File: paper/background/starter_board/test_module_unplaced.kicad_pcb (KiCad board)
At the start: 2 copper layers, 82.3 x 112.9 mm, 14 parts, among them J1 Barrel_Jack_12V, M1 ERM_Motor, M2 Stepper_4wire, M3 Servo_3pin, U1 D24V22F5_Buck, U2 Pi_Pico_W, U3 DRV2605L_Breakout, U4 DRV8871_Breakout, U5 Tic_T500

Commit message: Compact starter-board placement + emit unplaced auto-place variant trio
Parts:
- moved U3 94.3 mm to (157.2, 22.3)
- moved C3 94.3 mm to (128.3, 79.0)
- moved J1 94.3 mm to (101.8, 6.00)
- moved M1 94.3 mm to (100.4, 50.0)
- moved M2 94.3 mm to (100.4, 96.8)
- moved M3 94.3 mm to (114.3, 98.1)
- moved SR1 94.3 mm to (148.6, 79.8)
- moved U1 94.3 mm to (117.6, 5.58)
- moved U2 94.3 mm to (120.3, 29.8)
- moved U4 94.3 mm to (118.8, 60.2)
- moved U5 94.3 mm to (107.5, 83.0)
- moved C1 94.3 mm to (132.1, 4.75)
- moved C2 94.3 mm to (146.0, 4.75)
- moved SOL1 94.3 mm to (137.1, 50.0)
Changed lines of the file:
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@@
   (net 20 "VIB_B")
   (footprint "powder_doser_parts:Barrel_Jack_12V" (version 20221018) (generator kiutils) (layer "F.Cu")
-    (at 7.5 6.0 0)
+    (at 101.78 6.0 0)
     (fp_text reference "J1" (at 0 -6.5 0) (layer "F.SilkS")
       (effects (font (size 1.0 1.0) (thickness 0.15)))
@@
   )
   (footprint "powder_doser_parts:D24V22F5_Buck" (version 20221018) (generator kiutils) (layer "F.Cu")
-    (at 23.35 5.58 0)
+    (at 117.63 5.58 0)
     (fp_text reference "U1" (at 0 -6.08 0) (layer "F.SilkS")
       (effects (font (size 1.0 1.0) (thickness 0.15)))
@@
   )
   (footprint "powder_doser_parts:Cap_Polar" (version 20221018) (generator kiutils) (layer "F.Cu")
-    (at 37.86 4.75 0)
+    (at 132.14 4.75 0)
     (fp_text reference "C1" (at 0 -5.25 0) (layer "F.SilkS")
       (effects (font (size 1.0 1.0) (thickness 0.15)))
@@
   )
   (footprint "powder_doser_parts:Cap_Polar" (version 20221018) (generator kiutils) (layer "F.Cu")
-    (at 51.67999999999999 4.75 0)
+    (at 145.95999999999998 4.75 0)
     (fp_text reference "C2" (at 0 -5.25 0) (layer "F.SilkS")
       (effects (font (size 1.0 1.0) (thickness 0.15)))
@@
   )
   (footprint "powder_doser_parts:Pi_Pico_W" (version 20221018) (generator kiutils) (layer "F.Cu")
-    (at 26.0 29.82 0)
+    (at 120.28 29.82 0)
     (fp_text reference "U2" (at 0 -16.82 0) (layer "F.SilkS")
       (effects (font (size 1.0 1.0) (thickness 0.15)))
@@
   )
   (footprint "powder_doser_parts:DRV2605L_Breakout" (version 20221018) (generator kiutils) (layer "F.Cu")
-    (at 62.89 22.255000000000003 0)
+    (at 157.17000000000002 22.255000000000003 0)
     (fp_text reference "U3" (at 0 -9.255 0) (layer "F.SilkS")
       (effects (font (size 1.0 1.0) (thickness 0.15)))
@@
   )
   (footprint "powder_doser_parts:ERM_Motor" (version 20221018) (generator kiutils) (layer "F.Cu")
-    (at 6.16 49.99 0)
+    (at 100.44 49.99 0)
     (fp_text reference "M1" (at 0 -2.85 0) (layer "F.SilkS")
       (effects (font (size 1.0 1.0) (thickness 0.15)))
@@
   )
   (footprint "powder_doser_parts:DRV8871_Breakout" (version 20221018) (generator kiutils) (layer "F.Cu")
-    (at 24.48 60.205 0)
+    (at 118.76 60.205 0)
     (fp_text reference "U4" (at 0 -13.065 0) (layer "F.SilkS")
       (effects (font (size 1.0 1.0) (thickness 0.15)))
@@
   )
   (footprint "powder_doser_parts:Solenoid" (version 20221018) (generator kiutils) (layer "F.Cu")
-    (at 42.8 49.99 0)
+    (at 137.07999999999998 49.99 0)
     (fp_text reference "SOL1" (at 0 -2.85 0) (layer "F.SilkS")
       (effects (font (size 1.0 1.0) (thickness 0.15)))
@@
   )
   (footprint "powder_doser_parts:Tic_T500" (version 20221018) (generator kiutils) (layer "F.Cu")
-    (at 13.2 82.97 0)
+    (at 107.48 82.97 0)
     (fp_text reference "U5" (at 0 -9.2 0) (layer "F.SilkS")
       (effects (font (size 1.0 1.0) (thickness 0.15)))
@@
   )
   (footprint "powder_doser_parts:Cap_Polar" (version 20221018) (generator kiutils) (layer "F.Cu")
-    (at 34.06 79.02 0)
+    (at 128.34 79.02 0)
     (fp_text reference "C3" (at 0 -5.25 0) (layer "F.SilkS")
       (effects (font (size 1.0 1.0) (thickness 0.15)))
@@
   )
   (footprint "powder_doser_parts:Shunt_Regulator" (version 20221018) (generator kiutils) (layer "F.Cu")
-    (at 54.285 79.85 0)
+    (at 148.565 79.85 0)
     (fp_text reference "SR1" (at 0 -6.08 0) (layer "F.SilkS")
       (effects (font (size 1.0 1.0) (thickness 0.15)))
@@
   )
   (footprint "powder_doser_parts:Stepper_4wire" (version 20221018) (generator kiutils) (layer "F.Cu")
-    (at 6.16 96.78999999999999 0)
+    (at 100.44 96.78999999999999 0)
     (fp_text reference "M2" (at 0 -4.12 0) (layer "F.SilkS")
       (effects (font (size 1.0 1.0) (thickness 0.15)))
@@
   )
   (footprint "powder_doser_parts:Servo_3pin" (version 20221018) (generator kiutils) (layer "F.Cu")
-    (at 19.98 98.05999999999999 0)
+    (at 114.26 98.05999999999999 0)
     (fp_text reference "M3" (at 0 -5.390000000000001 0) (layer "F.SilkS")
       (effects (font (size 1.0 1.0) (thickness 0.15)))

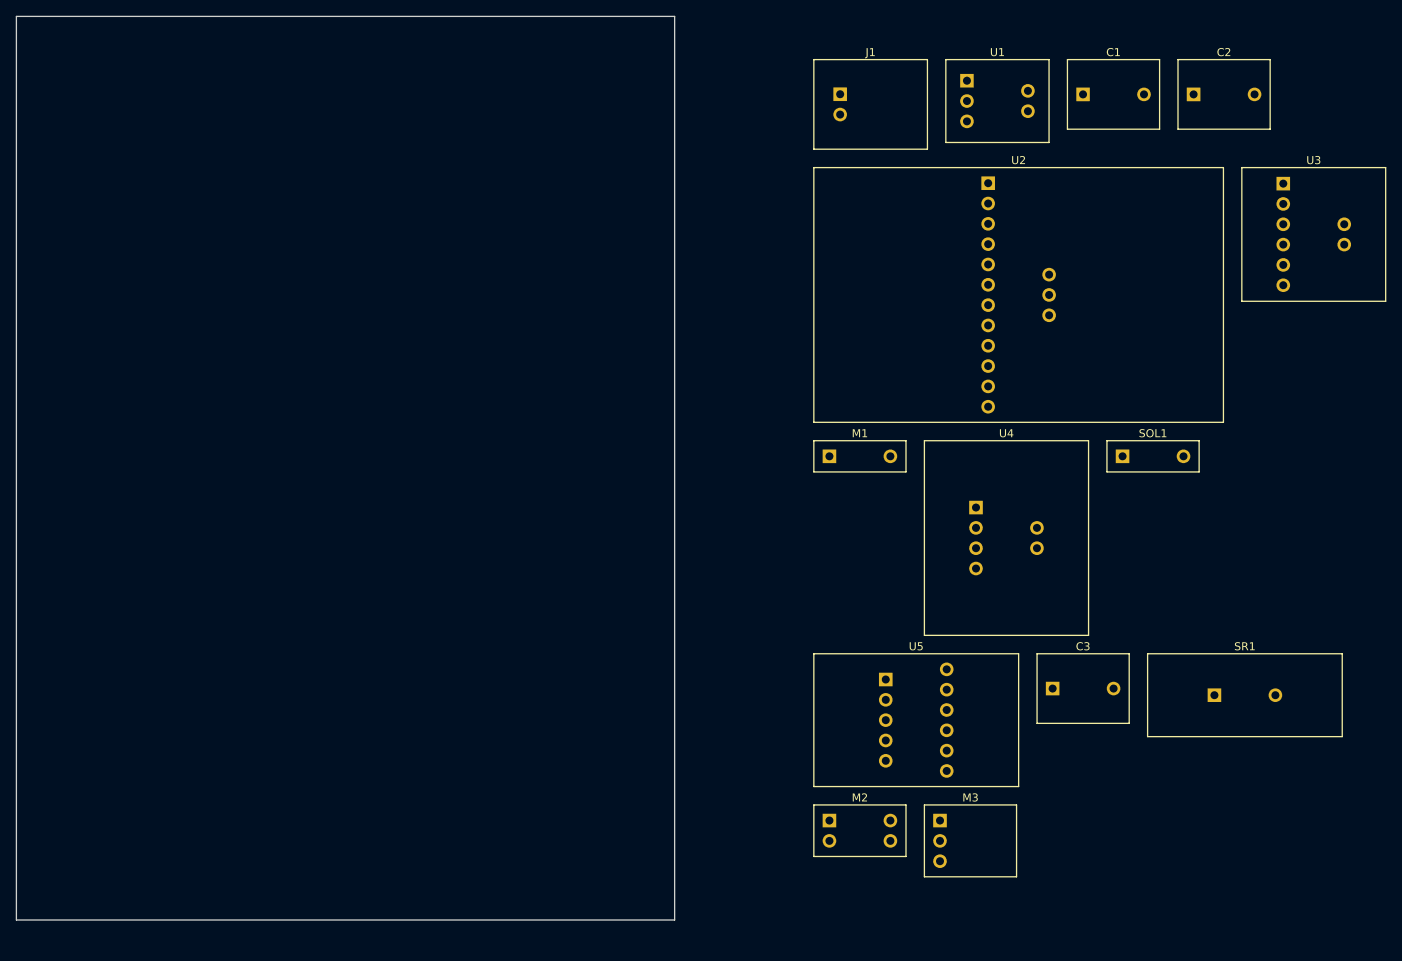
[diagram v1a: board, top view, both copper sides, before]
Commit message: Fix starter-board pin counts to match real parts (Pico W 15→40, etc.)
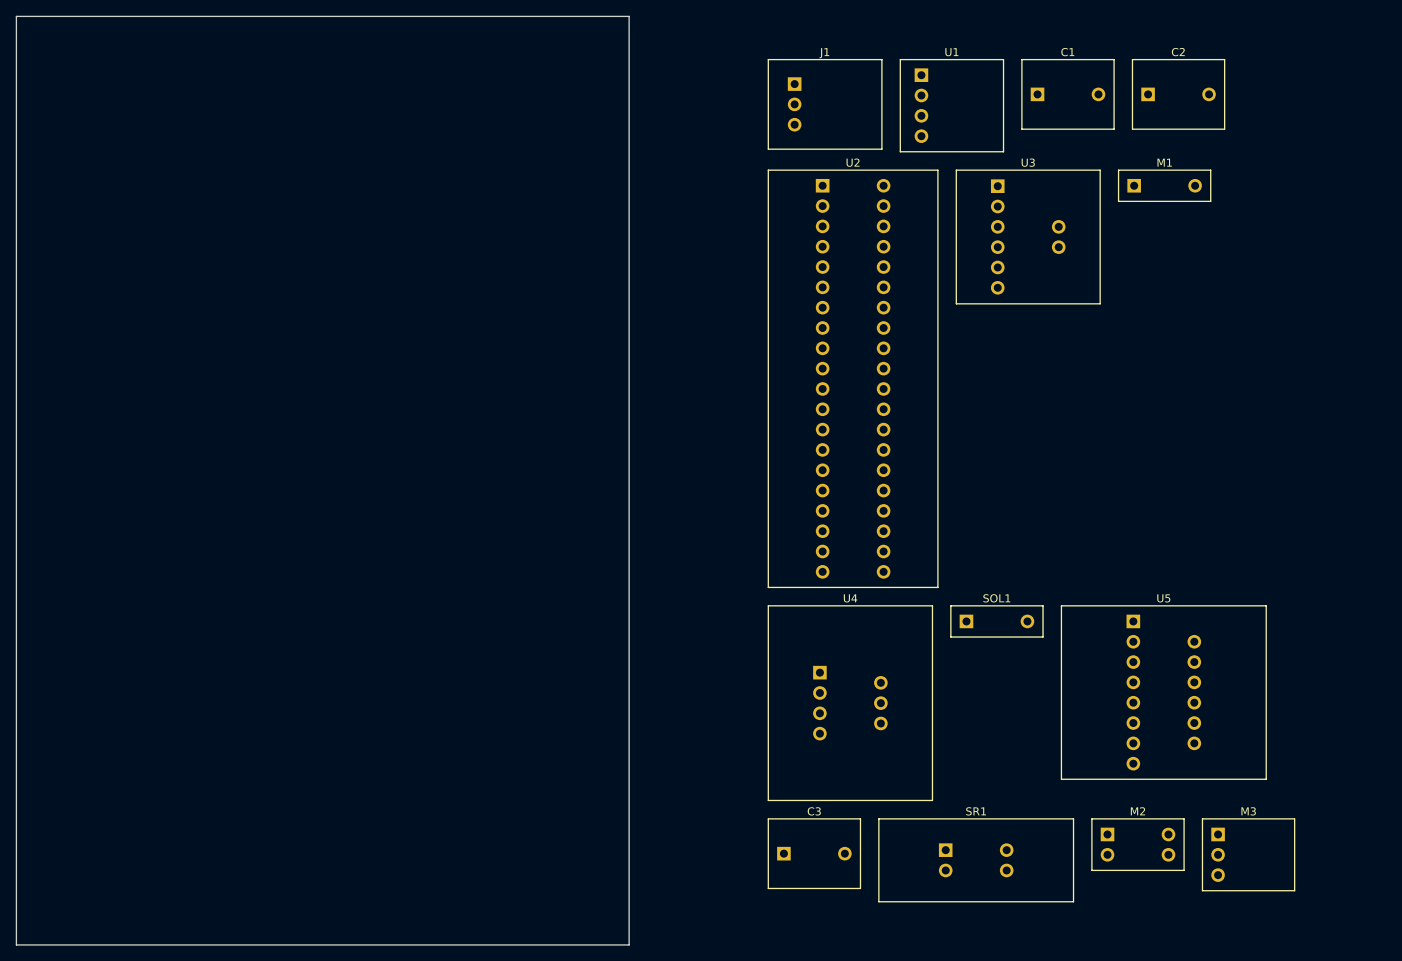
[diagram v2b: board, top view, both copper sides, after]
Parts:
- moved M1 50.9 mm to (138.5, 16.2)
- moved C3 39.4 mm to (94.8, 99.7)
- moved SR1 39.4 mm to (115.0, 100.5)
- moved U3 35.7 mm to (121.5, 22.6)
- moved M3 34.8 mm to (149.0, 99.8)
- moved M2 34.8 mm to (135.2, 98.5)
- moved U5 31.1 mm to (138.4, 79.5)
- moved U4 28.4 mm to (99.2, 80.8)
- moved SOL1 28.4 mm to (117.6, 70.6)
- moved U2 23.2 mm to (99.6, 40.3)
- moved U1 5.72 mm to (111.9, 6.16)
- moved C2 5.69 mm to (140.3, 4.75)
- moved J1 5.69 mm to (96.1, 6.00)
- moved C1 5.69 mm to (126.5, 4.75)
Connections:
- SR1 pad 2: GND -> +12V
- U1 pad 3: +12V -> +5V
- U1 pad 4: +5V -> +12V
- U2 pad 10: SOL_IN2 -> (no net)
- U2 pad 11: HAPT_EN -> (no net)
- U2 pad 12: SERVO_SIG -> (no net)
- U2 pad 13: +5V -> GND
- U2 pad 14: GND -> SOL_IN1
- U2 pad 15: +3V3 -> SOL_IN2
- U2 pad 3: (no net) -> GND
- U2 pad 5: STP_TX -> (no net)
- U2 pad 6: STP_RX -> STP_TX
- U2 pad 7: (no net) -> STP_RX
- U2 pad 8: (no net) -> GND
- U2 pad 9: SOL_IN1 -> (no net)
- U4 pad 3: SOL_IN1 -> SOL_A
- U4 pad 4: SOL_IN2 -> SOL_B
- U4 pad 5: SOL_A -> SOL_IN1
- U4 pad 6: SOL_B -> SOL_IN2
- U5 pad 10: STP_B1 -> GND
- U5 pad 11: STP_B2 -> STP_A1
- U5 pad 6: +12V -> (no net)
- U5 pad 8: STP_A1 -> (no net)
- U5 pad 9: STP_A2 -> +12V
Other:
- board size 82.3 x 112.9 mm -> 76.6 x 116.1 mm

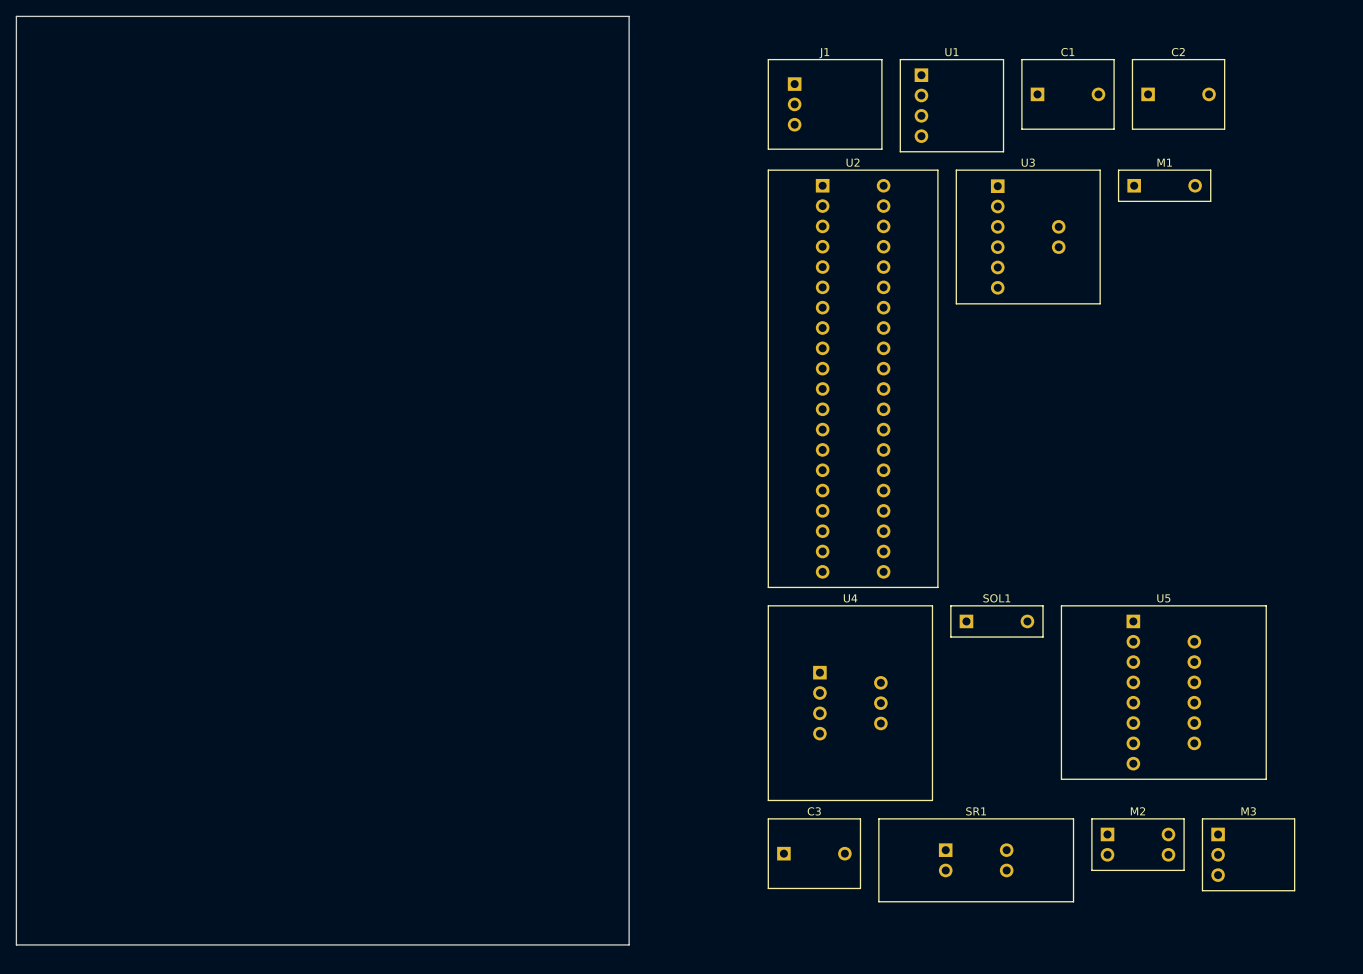
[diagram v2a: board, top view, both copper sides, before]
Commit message: Swap starter-board placeholder pads for real KiCad library footprints
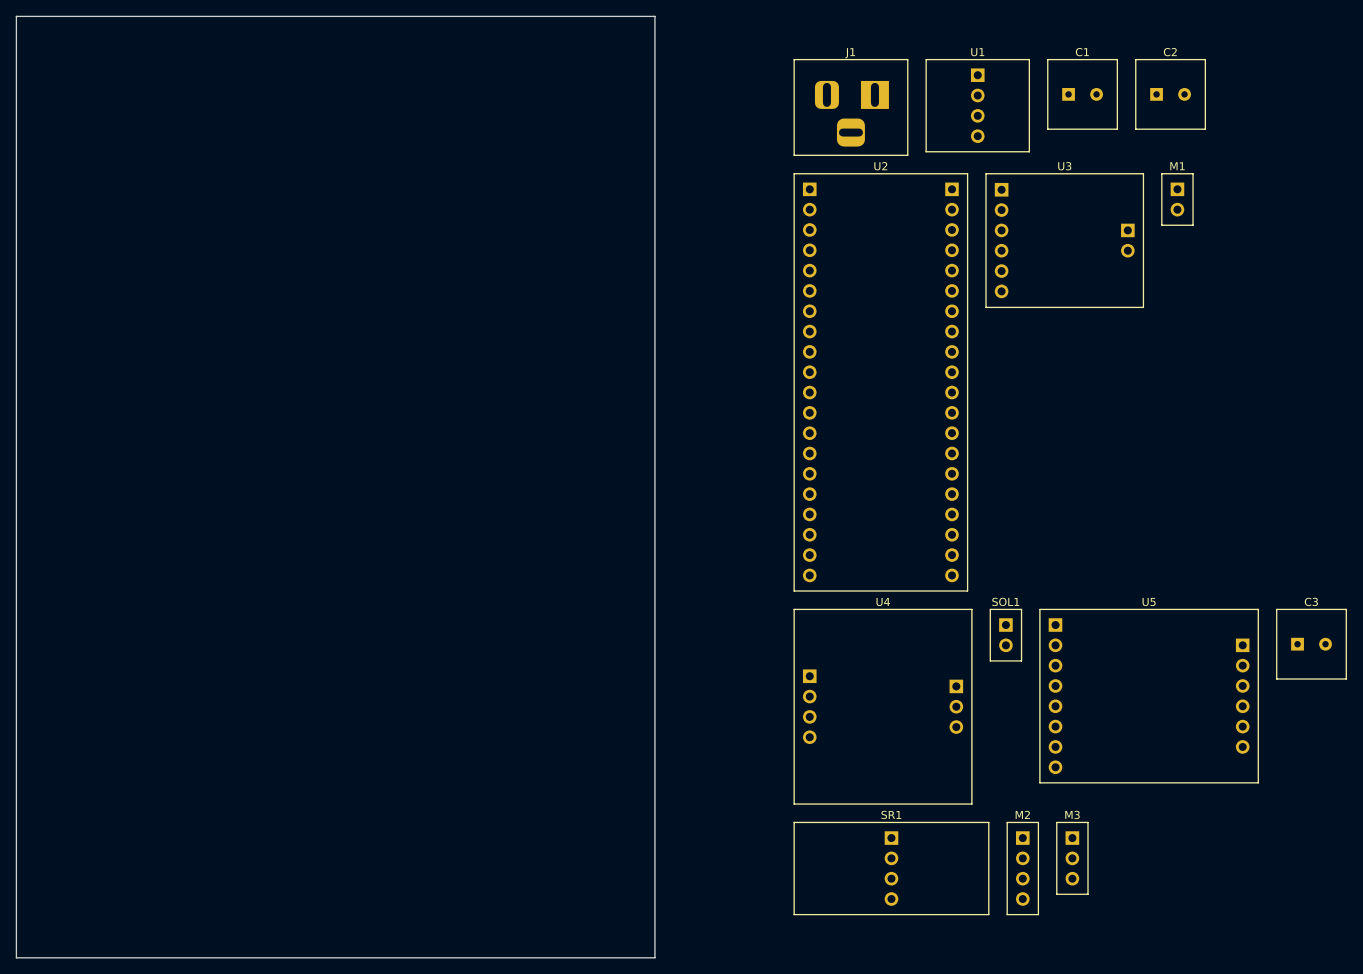
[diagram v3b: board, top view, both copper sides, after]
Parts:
- C1, C2, C3: footprint powder_doser_parts:Cap_Polar -> Capacitor_THT:CP_Radial_D8.0mm_P3.50mm
- J1: footprint powder_doser_parts:Barrel_Jack_12V -> Connector_BarrelJack:BarrelJack_Horizontal
- M1: footprint powder_doser_parts:ERM_Motor -> Connector_PinHeader_2.54mm:PinHeader_1x02_P2.54mm_Vertical
- M2: footprint powder_doser_parts:Stepper_4wire -> Connector_PinHeader_2.54mm:PinHeader_1x04_P2.54mm_Vertical
- M3: footprint powder_doser_parts:Servo_3pin -> Connector_PinHeader_2.54mm:PinHeader_1x03_P2.54mm_Vertical
- SOL1: footprint powder_doser_parts:Solenoid -> Connector_PinHeader_2.54mm:PinHeader_1x02_P2.54mm_Vertical
- moved C3 67.4 mm to (156.9, 73.5)
- moved M3 22.0 mm to (127.0, 100.2)
- moved M2 14.7 mm to (120.8, 101.5)
- moved SR1 10.6 mm to (104.4, 101.5)
- moved U3 4.58 mm to (126.0, 23.0)
- moved U4 4.10 mm to (103.3, 81.3)
- moved U2 3.50 mm to (103.1, 40.7)
- moved J1 3.25 mm to (99.3, 6.38)
- moved U1 3.23 mm to (115.2, 6.16)
- moved M1 2.35 mm to (140.1, 17.9)
- moved SOL1 2.05 mm to (118.7, 72.3)
- moved U5 1.89 mm to (136.6, 80.0)
- moved C1 1.82 mm to (128.3, 4.75)
- moved C2 1.00 mm to (139.3, 4.75)
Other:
- board size 76.6 x 116.1 mm -> 79.8 x 117.7 mm
